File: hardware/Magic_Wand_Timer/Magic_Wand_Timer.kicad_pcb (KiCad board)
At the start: 2 copper layers, 27.9 x 43.2 mm, 21 parts, among them J1 Conn_01x03, J2 Conn_01x03, J3 Conn_01x03, J4 Conn_01x02, Q1 AS2302, U1 MPM3610GQV-Z, U2 NE555D

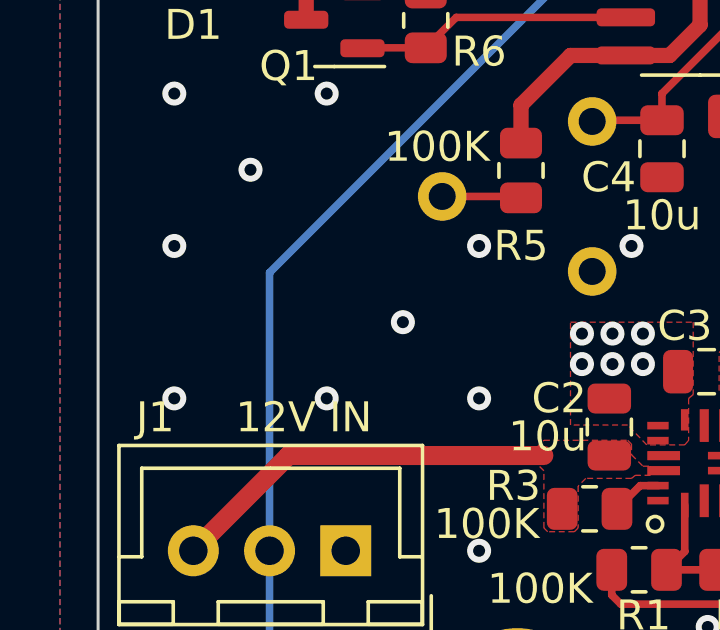
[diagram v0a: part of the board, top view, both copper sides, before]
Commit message: adding version text to Magic Wand PCB and generating new Gerbers and drill files
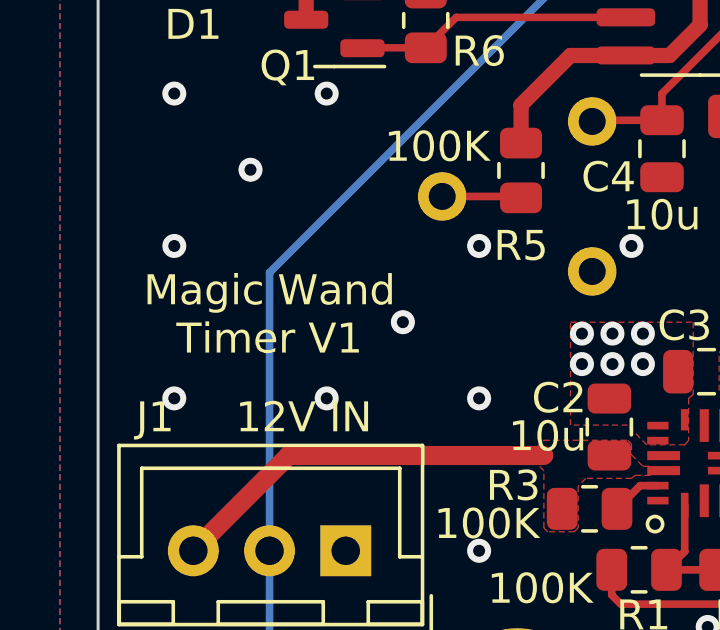
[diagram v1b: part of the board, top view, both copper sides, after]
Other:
- board text added: "Magic Wand Timer V1"
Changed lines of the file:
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@@
       (connect_pads (clearance 0))
       (min_thickness 0.254)
-      (keepout (tracks not_allowed) (vias not_allowed) (pads allowed ) (copperpour not_allowed) (footprints allowed))
+      (keepout (tracks not_allowed) (vias not_allowed) (pads allowed) (copperpour not_allowed) (footprints allowed))
       (fill (thermal_gap 0.508) (thermal_bridge_width 0.508))
       (polygon
@@
     (effects (font (size 1 1) (thickness 0.15)))
   )
+  (gr_text "Magic Wand \nTimer V1" (at 158.115 106.426) (layer "F.SilkS")
+    (effects (font (size 1 1) (thickness 0.15)))
+  )

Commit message: magic wand PCB updates
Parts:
- removed the J3 at (160.7, 121.3)
- removed the U1 at (173.5, 111.4)
- added Q1: SI2301CDS-T1-GE3, Package_TO_SOT_SMD:SOT-23, F.Cu at (168.4, 109.9)
- added R5: 10K, Resistor_SMD:R_0805_2012Metric, F.Cu at (163.6, 96.3)
- C2: value 10uF -> 1uF
- C3: value 22uF -> 10nF
- D1: value 1N4448W -> 1N4148W
- J1: value Conn_01x03 -> Action Input; footprint Useful Modifications:JST_XH_B3B-XH-A_1x03_P2.54mm_Vertical -> Connector_JST:JST_XH_B4B-XH-A_1x04_P2.50mm_Vertical
- J2: value Conn_01x03 -> Caddy In/Out; footprint Useful Modifications:JST_XH_B3B-XH-A_1x03_P2.54mm_Vertical -> Connector_JST:JST_XH_B4B-XH-A_1x04_P2.50mm_Vertical
- R1: value 100K -> 1K
- R2: value 19.1K -> 100K
- R4: value 10K -> 100K
- moved C2 14.4 mm to (165.6, 96.3)
- moved C3 13.1 mm to (167.6, 96.3), turned to 90 degrees
- moved R2 9.88 mm to (165.4, 109.9), turned to 90 degrees
- moved R1 8.70 mm to (163.3, 109.9), turned to 90 degrees
- moved R3 5.73 mm to (168.4, 107.2)
- moved J2 4.84 mm to (173.5, 118.0), turned to 90 degrees
- moved J1 4.47 mm to (158.2, 118.0), turned to 90 degrees
- moved R7 3.70 mm to (160.8, 99.4)
- moved Q2 3.66 mm to (157.8, 99.3)
- moved R6 1.40 mm to (167.1, 102.9), turned to 180 degrees
- moved C1 0.51 mm to (174.7, 99.8)
- moved C4 0.51 mm to (171.7, 100.9)
- moved R4 0.51 mm to (173.0, 92.2)
- moved U1 0.51 mm to (173.0, 95.9)
- moved D1 0.40 mm to (156.5, 95.0)
- renumbered J4 to J3, Q1 to Q2, R5 to R6, R6 to R7, U2 to U1
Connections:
- C2 pad 1: +12V -> GND
- C2 pad 2: GND -> Filtered_Input
- C3 pad 1: +5V -> GND
- C3 pad 2: GND -> Filtered_Input
- J1 pad 1: GND -> +12V
- J1 pad 2: Trigger -> +5V
- J1 pad 3: +12V -> GND
- J2 pad 1: GND -> +12V
- J2 pad 2: Trigger -> +5V
- J2 pad 3: +5V -> GND
- R1 pad 1: +5V -> Trigger
- R1 pad 2: Net-(R1-Pad2) -> Net-(Q1-G)
- R2 pad 1: Net-(R1-Pad2) -> +5V
- R2 pad 2: Net-(R2-Pad2) -> Net-(Q1-G)
- R3 pad 1: Net-(R3-Pad1) -> Caddy_Trigger
- R3 pad 2: +12V -> GND
- R4 pad 2: Trigger -> Filtered_Input
- U1 pad 2: Trigger -> Filtered_Input
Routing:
- net Trigger: track 54.4 -> 20.8 mm, vias 1 -> 2
- net +5V: track 110.3 -> 98.0 mm
- net Filtered_Input: track 0.00 -> 11.4 mm
- net Caddy_Trigger: track 0.00 -> 7.13 mm
- net Output: track 9.23 -> 13.7 mm
- net Net-(Q1-G): track 0.00 -> 4.16 mm
- net Net-(R1-Pad2): track 4.02 -> 0.00 mm
- net +12V: track 13.4 -> 17.1 mm
- net Net-(R2-Pad2): track 2.93 -> 0.00 mm
- net Net-(D1-A): track 6.43 -> 9.02 mm
- net Net-(R3-Pad1): track 1.69 -> 0.00 mm
- net Net-(U1-DIS): track 10.8 -> 11.3 mm
- net GND: track 0.32 -> 0.00 mm, vias 42 -> 53
- removed copper zone on F.Cu, net +12V
- removed copper zone on F.Cu, net +5V
- removed copper zone on F.Cu, net Net-(U1-Pad4)
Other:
- board text added: "Btn"
- board text added: "Caddy"
- board text added: "Magic Wand Timer V2"
- board text added: "Trig"
- board text removed: "100K"
- board text removed: "10K"
- board text removed: "10n"
- board text removed: "10u"
- board text removed: "12V IN"
- board text removed: "19.1K"
- board text removed: "22u"
- board text removed: "5V IN"
- board text removed: "Button"
- board text removed: "Magic Wand Timer V1"
- board text removed: "S"

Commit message: Magic Wand Timer Updates
Added 12V/5V switching, SMD/THT potentiometer options, Delayed start to handle erratic comparator behavior
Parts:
- added C2: 10uF, Capacitor_SMD:C_0805_2012Metric, F.Cu at (168.4, 107.2)
- added D1: 1N4148W, Diode_SMD:D_SOD-123, F.Cu at (175.0, 106.4)
- added Q2: MMBT5551L, Package_TO_SOT_SMD:SOT-23, F.Cu at (174.0, 103.3)
- added R10: 0, Resistor_SMD:R_0805_2012Metric, F.Cu at (157.0, 105.2)
- added R11: 0, Resistor_SMD:R_0805_2012Metric, F.Cu at (157.0, 103.1)
- added R6: 1K, Resistor_SMD:R_0805_2012Metric, F.Cu at (171.2, 105.7)
- added R7: 100K, Resistor_SMD:R_0805_2012Metric, F.Cu at (176.8, 102.2)
- added RV2: 500K, Potentiometer_SMD:Potentiometer_Bourns_TC33X_Vertical, F.Cu at (167.4, 102.5)
- moved R8 3.64 mm to (165.6, 106.2), turned to 90 degrees
- moved Q1 2.10 mm to (168.4, 112.0)
- moved R1 2.10 mm to (163.3, 112.0)
- moved R2 2.10 mm to (165.4, 112.0)
- moved R3 2.10 mm to (168.4, 109.3)
- moved C5 0.51 mm to (171.2, 100.9)
- moved C1 0.32 mm to (174.5, 99.6)
- renumbered C2 to C3, C3 to C4, C4 to C5, D1 to D2, Q2 to Q3, R6 to R8, R7 to R9
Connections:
- D2 pad 1: +5V -> Net-(D2-K)
- J3 pad 2: +5V -> Net-(D2-K)
- U1 pad 4: +5V -> ON_Delay
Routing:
- net +5V: track 98.0 -> 59.9 mm
- net +12V: track 17.1 -> 35.3 mm
- net Net-(D2-K): track 0.00 -> 16.0 mm
- net Trigger: track 20.8 -> 15.6 mm
- net Caddy_Trigger: track 7.13 -> 2.74 mm
- net Net-(R8-Pad2): track 2.51 -> 0.18 mm
- net GND: vias 53 -> 44

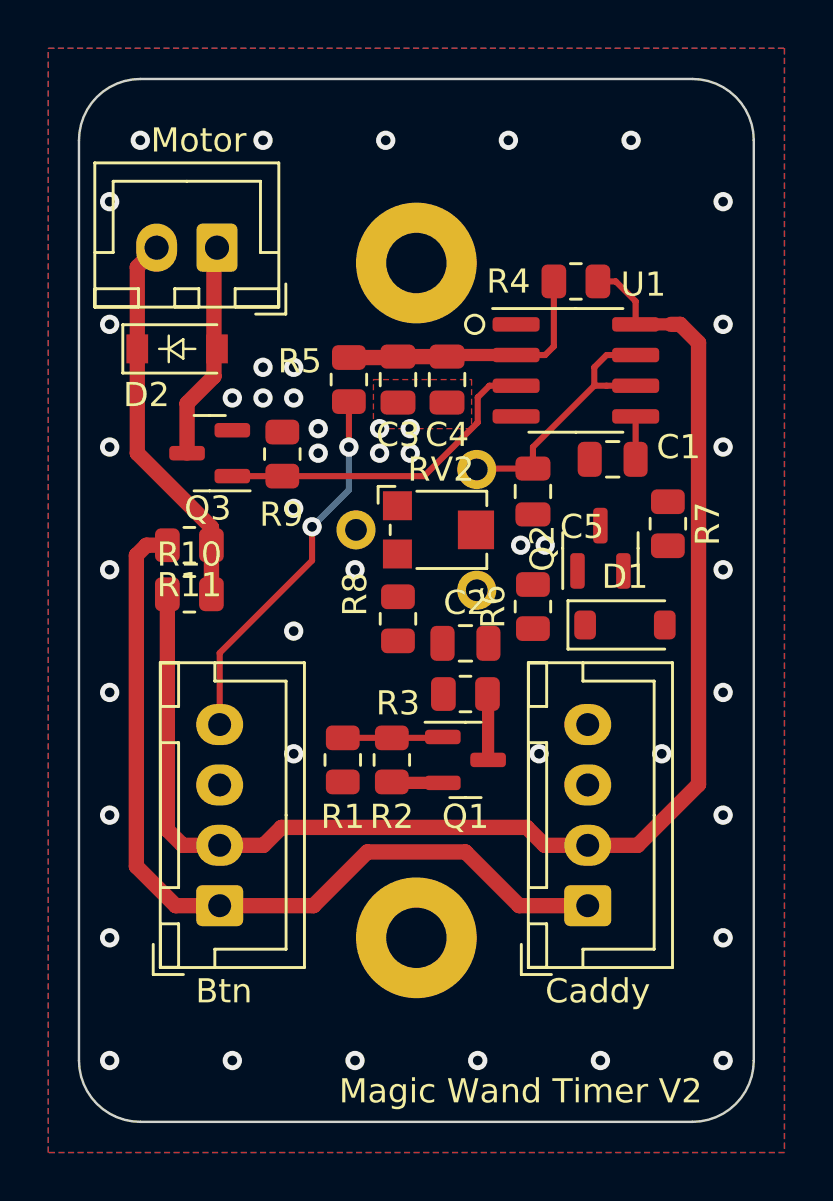
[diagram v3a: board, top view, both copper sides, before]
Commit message: Wand Timer V3 Routing
Finished routing components for V3 Magic Wand Timer
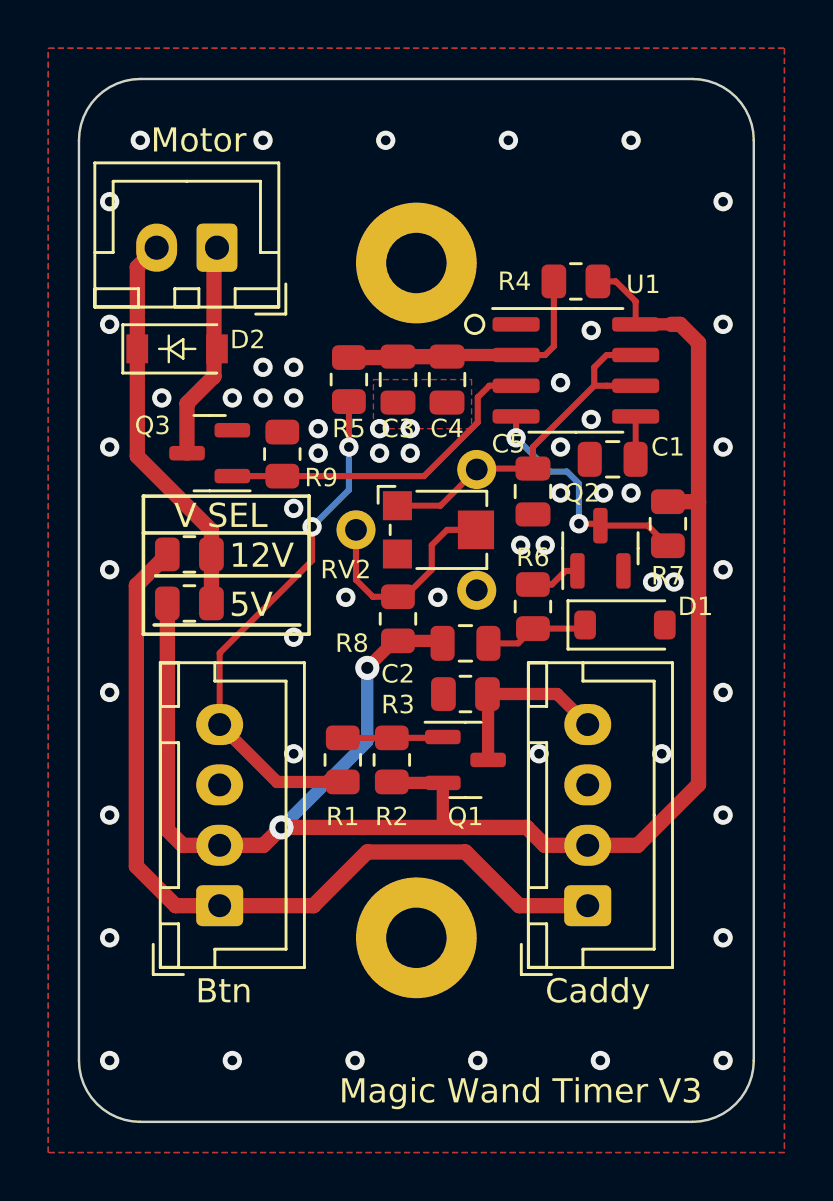
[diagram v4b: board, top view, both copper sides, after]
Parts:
- moved R10 0.38 mm to (157.0, 105.5)
- moved R11 0.38 mm to (157.0, 103.5)
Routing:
- net +5V: track 59.9 -> 74.3 mm, vias 0 -> 2
- net ON_Delay: track 0.00 -> 10.00 mm, vias 0 -> 2
- net Net-(R8-Pad2): track 0.18 -> 9.25 mm
- net Trigger: track 15.6 -> 21.7 mm
- net Caddy_Trigger: track 2.74 -> 7.41 mm
- net Net-(D1-K): track 0.00 -> 4.32 mm
- net Net-(U1-DIS): track 11.2 -> 15.1 mm
- net Net-(Q2-B): track 0.00 -> 2.08 mm
- net +12V: track 35.3 -> 34.7 mm
- net GND: vias 44 -> 55
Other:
- board text added: "Magic Wand Timer V3"
- board text added: "V SEL"
- board text removed: "Magic Wand Timer V2"
